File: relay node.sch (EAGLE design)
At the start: 27 parts, among them J2 LED, J3 PROG, J4 Relays, J5 AUX, U1 ESP-WROOM-02U, U2 MCP23017SO, U3 ULN2803ADWRG4, U4 ULN2803ADWRG4, U5 TLV75533PDBVR

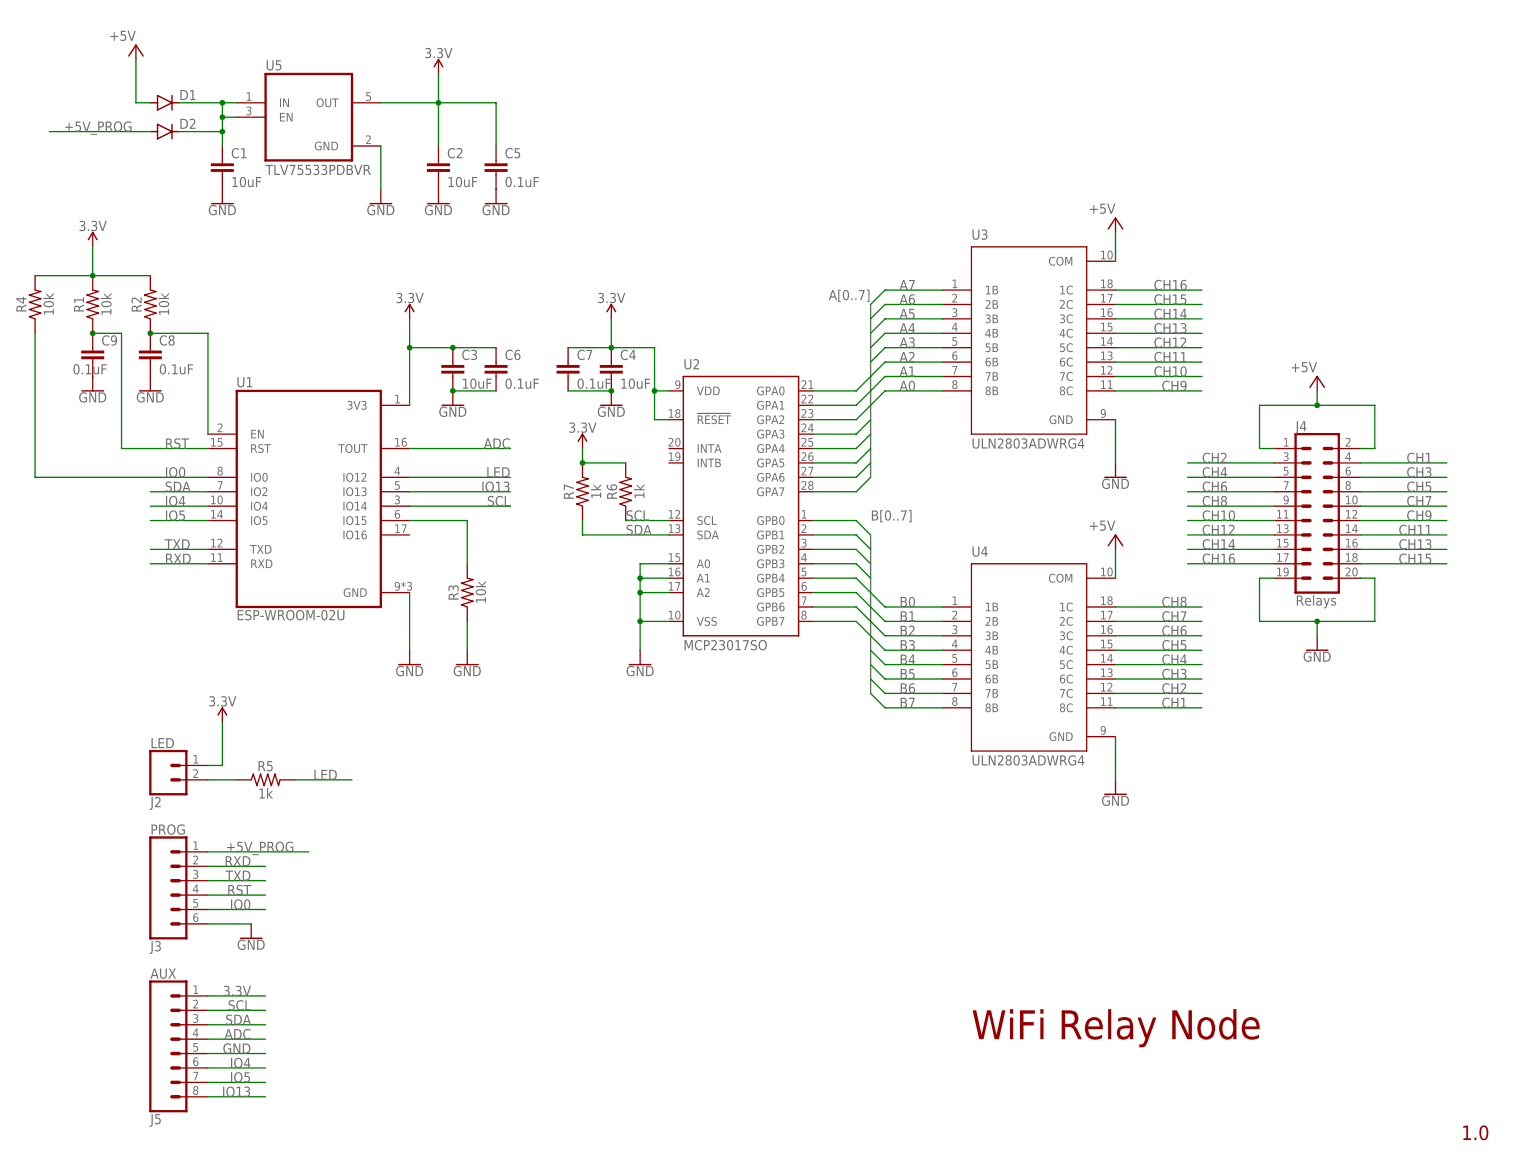
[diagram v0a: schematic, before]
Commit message: Edited wifi IC footprint - Removed solder mask and solder paste (tcream layer) from esp-wroom IC -Updated BOM
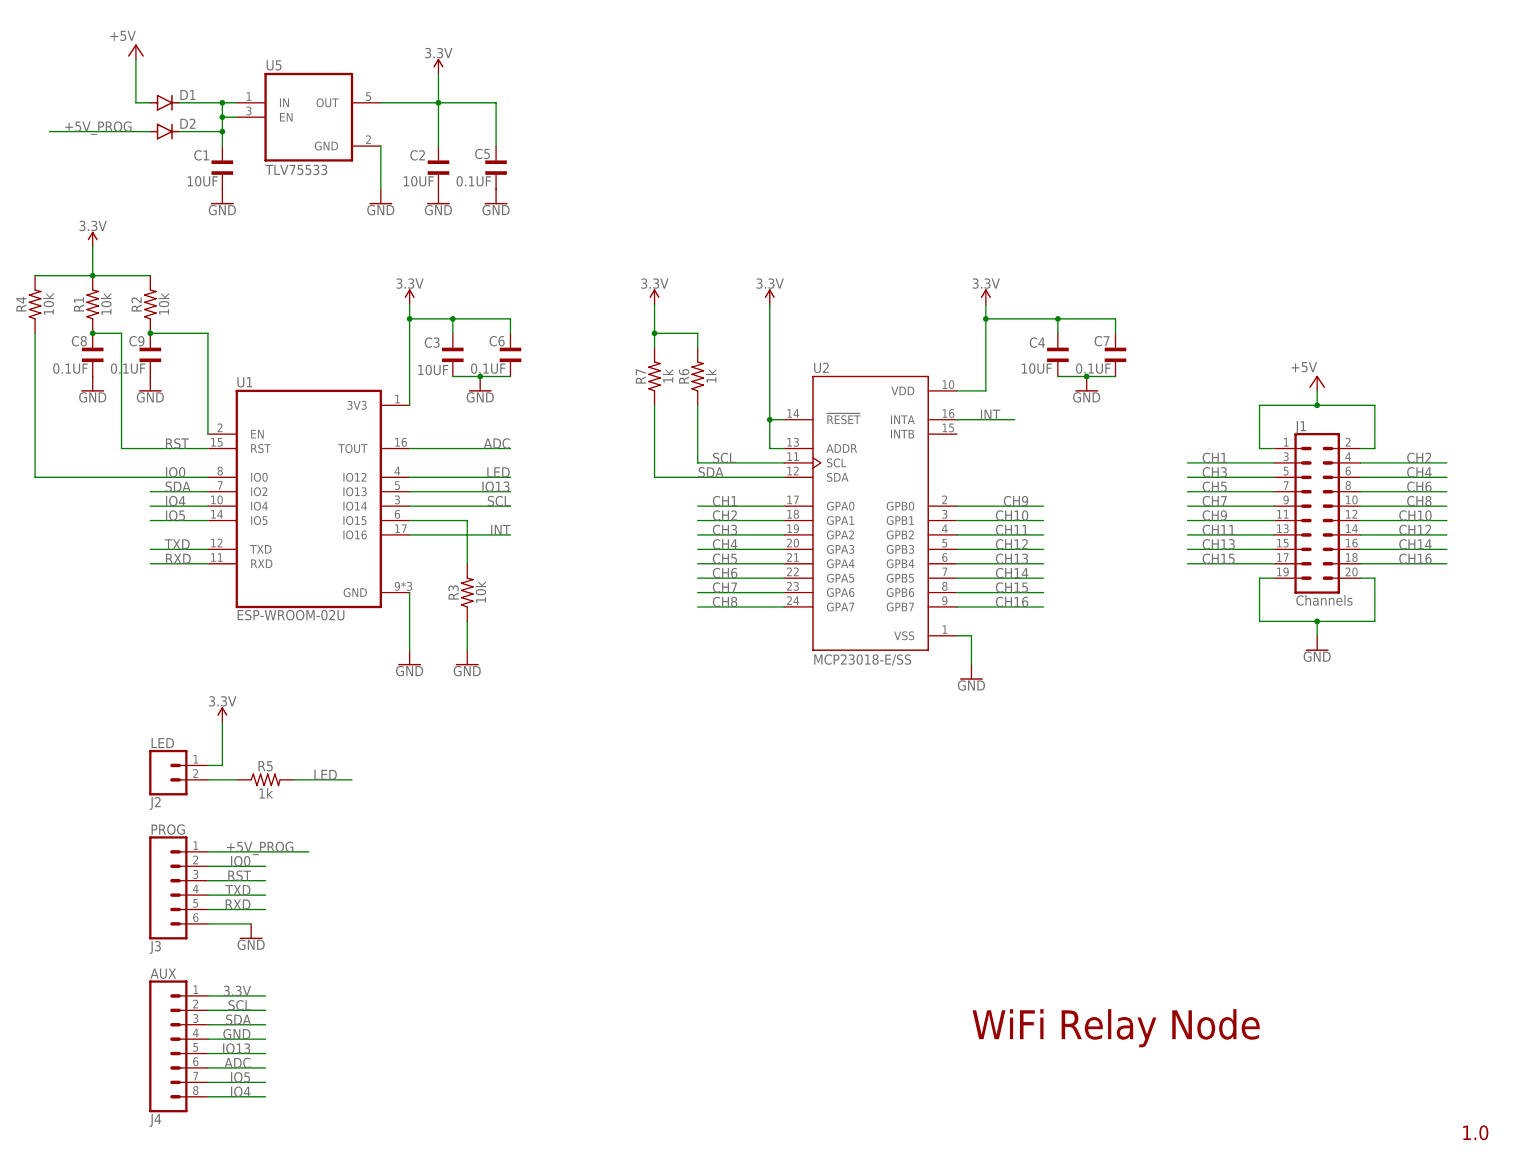
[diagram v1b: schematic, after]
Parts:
- removed J5: AUX, SFM-Project:CONN_08"
- removed U3, U4: ULN2803ADWRG4, SFM-Project:ULN2803ADWRG4
- added J1: Channels, SFM-Project:CONN_10X2NOSILK
- C1, C2, C3, C4: value 10uF -> 10UF; device SFM-Project:10UF-0805-25V-10% -> SFM-Project:10UF
- C5, C6, C7, C8, C9: value 0.1uF -> 0.1UF; device SFM-Project:0.1UF-0603-25V-5% -> SFM-Project:0.1UF
- J4: value Relays -> AUX; device SFM-Project:CONN_10X2 -> SFM-Project:CONN_08"
- U2: value MCP23017SO -> MCP23018-E/SS; device SFM-Project:MCP23017SO -> SFM-Project:MCP23018-E/SS
- U5: value TLV75533PDBVR -> TLV75533
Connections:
- removed net A0: U2.GPA0, U3.8B
- removed net A1: U2.GPA1, U3.7B
- removed net A2: U2.GPA2, U3.6B
- removed net A3: U2.GPA3, U3.5B
- removed net A4: U2.GPA4, U3.4B
- removed net A5: U2.GPA5, U3.3B
- removed net A6: U2.GPA6, U3.2B
- removed net A7: U2.GPA7, U3.1B
- removed net B0: U2.GPB0, U4.1B
- removed net B1: U2.GPB1, U4.2B
- removed net B2: U2.GPB2, U4.3B
- removed net B3: U2.GPB3, U4.4B
- removed net B4: U2.GPB4, U4.5B
- removed net B5: U2.GPB5, U4.6B
- removed net B6: U2.GPB6, U4.7B
- removed net B7: U2.GPB7, U4.8B
- removed net N$5: C8.1, R2.1, U1.EN
- new net INT: U1.IO16, U2.INTA
- new net N$3: C9.1, R2.1, U1.EN
- net +5V: now also J1.1, J1.2; no longer J4.1, J4.2, U3.COM, U4.COM
- net 3.3V: now also J4.1, U2.ADDR; no longer J5.1
- net ADC: now also J4.6; no longer J5.4
- net CH1: now also J1.3, U2.GPA0; no longer J4.4, U4.8C
- net CH10: now also J1.12, U2.GPB1; no longer J4.11, U3.7C
- net CH11: now also J1.13, U2.GPB2; no longer J4.14, U3.6C
- net CH12: now also J1.14, U2.GPB3; no longer J4.13, U3.5C
- net CH13: now also J1.15, U2.GPB4; no longer J4.16, U3.4C
- net CH14: now also J1.16, U2.GPB5; no longer J4.15, U3.3C
- net CH15: now also J1.17, U2.GPB6; no longer J4.18, U3.2C
- net CH16: now also J1.18, U2.GPB7; no longer J4.17, U3.1C
- net CH2: now also J1.4, U2.GPA1; no longer J4.3, U4.7C
- net CH3: now also J1.5, U2.GPA2; no longer J4.6, U4.6C
- net CH4: now also J1.6, U2.GPA3; no longer J4.5, U4.5C
- net CH5: now also J1.7, U2.GPA4; no longer J4.8, U4.4C
- net CH6: now also J1.8, U2.GPA5; no longer J4.7, U4.3C
- net CH7: now also J1.9, U2.GPA6; no longer J4.10, U4.2C
- net CH8: now also J1.10, U2.GPA7; no longer J4.9, U4.1C
- net CH9: now also J1.11, U2.GPB0; no longer J4.12, U3.8C
- net GND: now also J1.19, J1.20, J4.4; no longer J4.19, J4.20, J5.5, U2.A0, U2.A1, U2.A2, U3.GND, U4.GND
- net IO0: now also J3.2; no longer J3.5
- net IO13: now also J4.5; no longer J5.8
- net IO4: now also J4.8; no longer J5.6
- net IO5: now also J4.7; no longer J5.7
- net RST: now also C8.1, J3.3; no longer C9.1, J3.4
- net RXD: now also J3.5; no longer J3.2
- net SCL: now also J4.2; no longer J5.2
- net SDA: now also J4.3; no longer J5.3
- net TXD: now also J3.4; no longer J3.3
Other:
- moved on the sheet: R6, R7

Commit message: Minor changes
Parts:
- renumbered U5 to U3
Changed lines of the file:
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@@
 <part name="GND2" library="SparkFun-PowerSymbols" deviceset="GND" device=""/>
 <part name="GND8" library="SparkFun-PowerSymbols" deviceset="GND" device=""/>
-<part name="U5" library="SFM-Project" deviceset="TLV75533PDBVR" device="" value="TLV75533"/>
+<part name="U3" library="SFM-Project" deviceset="TLV75533PDBVR" device="" value="TLV75533"/>
 <part name="GND7" library="SparkFun-PowerSymbols" deviceset="GND" device=""/>
 <part name="P+4" library="supply1" library_urn="urn:adsk.eagle:library:371" deviceset="+5V" device=""/>
@@
 <attribute name="VALUE" x="83.82" y="172.466" size="1.778" layer="96" align="top-center"/>
 </instance>
-<instance part="U5" gate="G$1" x="60.96" y="187.96" smashed="yes">
+<instance part="U3" gate="G$1" x="60.96" y="187.96" smashed="yes">
 <attribute name="NAME" x="53.33781875" y="196.21736875" size="1.778509375" layer="95"/>
 <attribute name="VALUE" x="53.324809375" y="177.7797" size="1.78155" layer="96"/>
@@
 <junction x="83.82" y="190.5"/>
 <pinref part="SUPPLY2" gate="G$1" pin="3.3V"/>
-<pinref part="U5" gate="G$1" pin="OUT"/>
+<pinref part="U3" gate="G$1" pin="OUT"/>
 <wire x1="93.98" y1="190.5" x2="83.82" y2="190.5" width="0.1524" layer="91"/>
 <pinref part="C2" gate="G$1" pin="1"/>
@@
 <wire x1="73.66" y1="182.88" x2="73.66" y2="175.26" width="0.1524" layer="91"/>
 <pinref part="GND2" gate="1" pin="GND"/>
-<pinref part="U5" gate="G$1" pin="GND"/>
+<pinref part="U3" gate="G$1" pin="GND"/>
 </segment>
 <segment>
@@
 <net name="N$1" class="0">
 <segment>
-<pinref part="U5" gate="G$1" pin="IN"/>
+<pinref part="U3" gate="G$1" pin="IN"/>
 <pinref part="D1" gate="G$1" pin="C"/>
 <wire x1="48.26" y1="190.5" x2="45.72" y2="190.5" width="0.1524" layer="91"/>
@@
 <wire x1="45.72" y1="185.42" x2="45.72" y2="187.96" width="0.1524" layer="91"/>
 <wire x1="48.26" y1="187.96" x2="45.72" y2="187.96" width="0.1524" layer="91"/>
-<pinref part="U5" gate="G$1" pin="EN"/>
+<pinref part="U3" gate="G$1" pin="EN"/>
 <pinref part="D2" gate="G$1" pin="C"/>
 <wire x1="38.1" y1="185.42" x2="45.72" y2="185.42" width="0.1524" layer="91"/>
